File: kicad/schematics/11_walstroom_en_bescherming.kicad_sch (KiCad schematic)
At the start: 6 parts

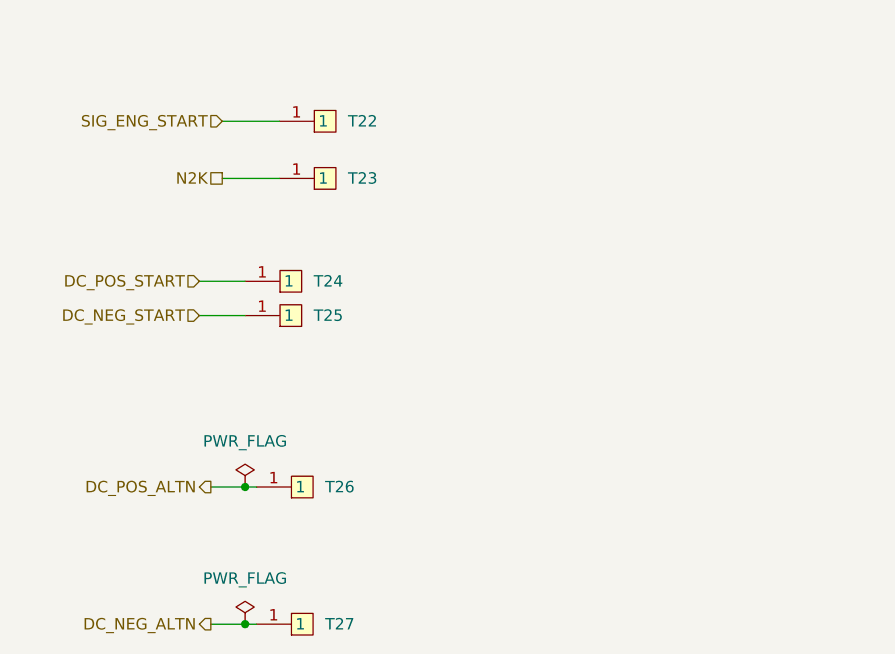
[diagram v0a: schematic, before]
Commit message: Introductie schema 15_energieconversie
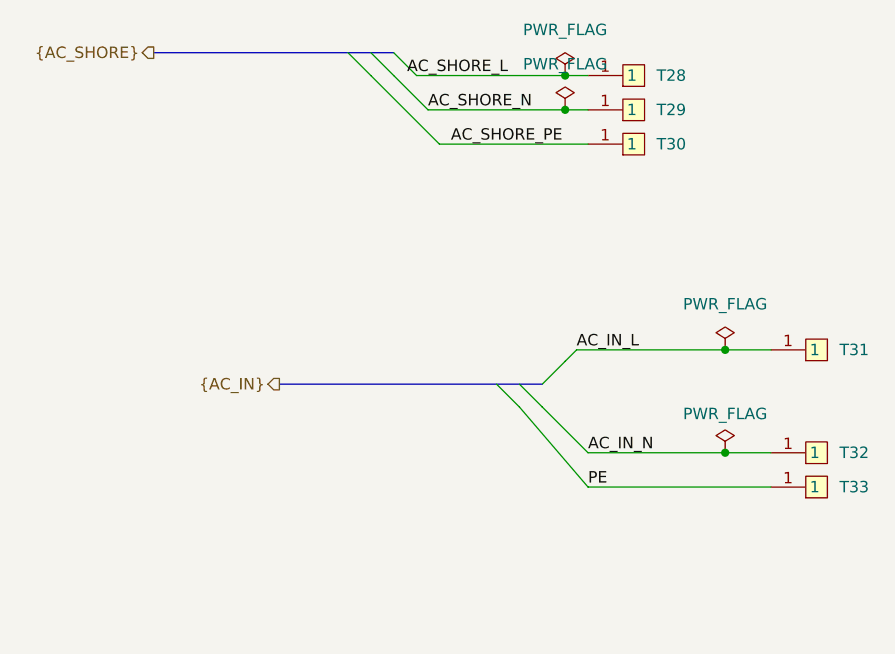
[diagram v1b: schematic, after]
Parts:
- removed T22, T23: (no value), symbol falkor-electrical:IF_Passief
- removed T24, T25, T26, T27: (no value), symbol falkor-electrical:IF_Power_Input
- added T28, T29, T31, T32: (no value), symbol falkor-electrical:IF_Power_Input
- added T30, T33: (no value), symbol falkor-electrical:IF_Passief
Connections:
- new net AC_IN_L: T31.1
- new net AC_IN_N: T32.1
- new net AC_SHORE_L: T28.1
- new net AC_SHORE_N: T29.1
- new net AC_SHORE_PE: T30.1
- new net PE: T33.1
